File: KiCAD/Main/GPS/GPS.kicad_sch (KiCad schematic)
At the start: 16 parts, among them U1 MAX-M8Q, U2 PHA-23LN

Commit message: Fix labeling issue
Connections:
- net GPS RESET renamed GPS_RESET
- net GPS UART RX renamed GPS_UART_RX
- net GPS UART TX renamed GPS_UART_TX
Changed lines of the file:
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@@
 		)
 	)
-	(global_label "GPS UART TX"
+	(hierarchical_label "GPS_UART_TX"
 		(shape input)
 		(at 73.66 68.58 180)
-		(fields_autoplaced yes)
 		(effects
 			(font
@@
 			(justify right)
 		)
-		(property "Intersheetrefs" "${INTERSHEET_REFS}"
-			(at 58.1563 68.58 0)
-			(effects
-				(font
-					(size 1.27 1.27)
-				)
-				(justify right)
-				(hide yes)
-			)
-		)
 	)
-	(global_label "GPS UART RX"
+	(hierarchical_label "GPS_RESET"
 		(shape input)
-		(at 73.66 66.04 180)
-		(fields_autoplaced yes)
+		(at 80.01 88.9 180)
 		(effects
 			(font
@@
 			(justify right)
 		)
-		(property "Intersheetrefs" "${INTERSHEET_REFS}"
-			(at 57.8539 66.04 0)
-			(effects
-				(font
-					(size 1.27 1.27)
-				)
-				(justify right)
-				(hide yes)
-			)
-		)
 	)
-	(global_label "GPS RESET"
+	(hierarchical_label "GPS_UART_RX"
 		(shape input)
-		(at 80.01 88.9 180)
-		(fields_autoplaced yes)
+		(at 73.66 66.04 180)
 		(effects
 			(font
@@
 			(justify right)
 		)
-		(property "Intersheetrefs" "${INTERSHEET_REFS}"
-			(at 66.5626 88.9 0)
-			(effects
-				(font
-					(size 1.27 1.27)
-				)
-				(justify right)
-				(hide yes)
-			)
-		)
 	)

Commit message: Continue integrating
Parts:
- added AE2: Antenna, symbol Device:Antenna
- added C12: 0.001u, symbol Device:C
- added C13, C15, C16: 0.1u, symbol Device:C
- added C14: 0.01u, symbol Device:C
- added C17: 1.2p, symbol Device:C
- added IC1: E22-900M22S, E22-900M22S:E22-900M22S, symbol E22-900M22S:E22-900M22S
- added L3: 0.68u, symbol Device:L
- added L4: 1n, symbol Device:L
- added R5: 1.21k, symbol Device:R
- added U7: PHA-23LN, Package_TO_SOT_SMD:SOT-89-3, symbol RF_Amplifier:PHA-23LN
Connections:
- net GND: now also C13.1, C14.1, C17.2, L3.1, U7.2 (GND)
- new net: C13.2, C14.2, IC1.9 (VCC)
- new net: C15.1, R5.1
- new net: C12.2, L3.2, R5.2, U7.3
- new net: AE2.1 (A), C17.1, L4.2
- new net: C12.1, IC1.21 (ANT)
- new net: C15.2, C16.2, U7.1
- new net: C16.1, L4.1
- new net: IC1.1 (GND), IC1.10 (GND), IC1.11 (GND), IC1.12 (GND), IC1.2 (GND), IC1.20 (GND), IC1.22 (GND), IC1.3 (GND), IC1.4 (GND), IC1.5 (GND)
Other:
- moved on the sheet: AE1, C1, C2, C3, C4, C5, C6, JP1, L1, L2, R1, R2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

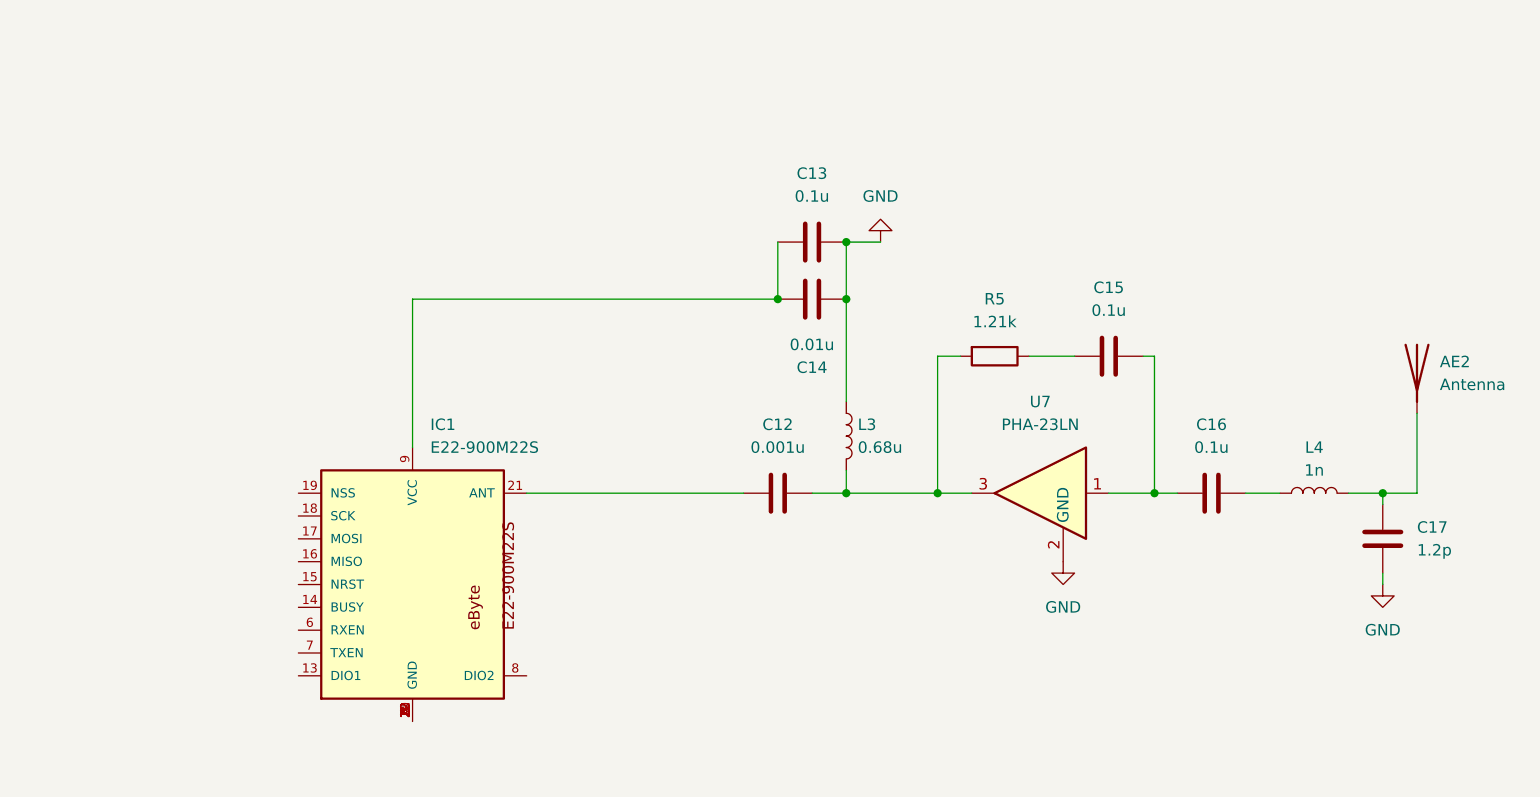
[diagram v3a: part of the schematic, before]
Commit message: Stable update. Begin fixing previous commit errors
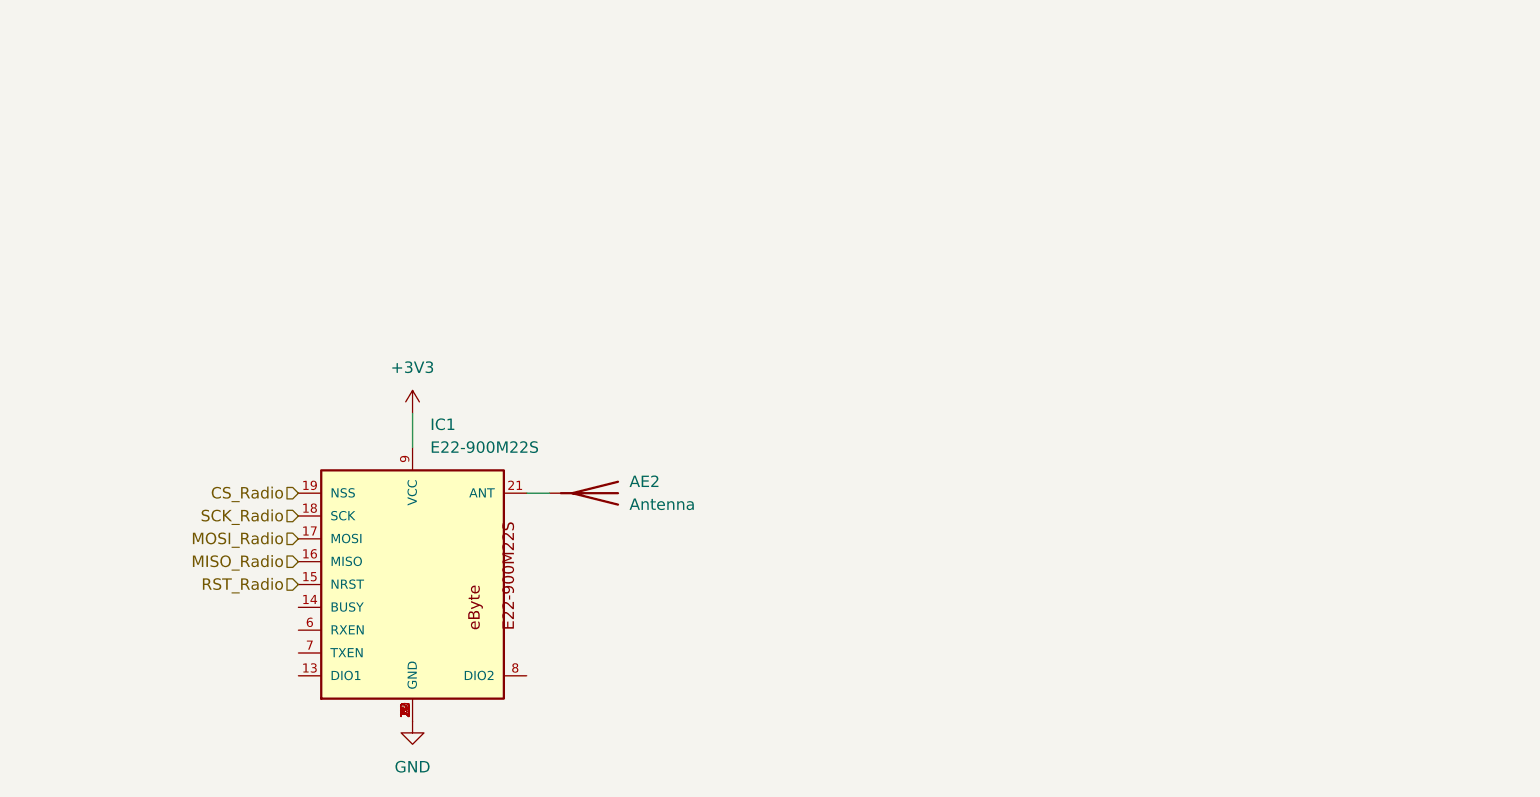
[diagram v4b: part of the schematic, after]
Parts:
- removed C12: 0.001u, symbol Device:C
- removed C13, C15, C16: 0.1u, symbol Device:C
- removed C14: 0.01u, symbol Device:C
- removed C17: 1.2p, symbol Device:C
- removed L3: 0.68u, symbol Device:L
- removed L4: 1n, symbol Device:L
- removed R5: 1.21k, symbol Device:R
- removed U7: PHA-23LN, Package_TO_SOT_SMD:SOT-89-3, symbol RF_Amplifier:PHA-23LN
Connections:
- net +3V3: now also IC1.9 (VCC)
- net GND: now also IC1.1 (GND), IC1.10 (GND), IC1.11 (GND), IC1.12 (GND), IC1.2 (GND), IC1.20 (GND), IC1.22 (GND), IC1.3 (GND), IC1.4 (GND), IC1.5 (GND)
- net at AE2.1 (A): now also IC1.21 (ANT)
- net RST_Radio: now reaches IC1.15 (NRST)
- net MISO_Radio: now reaches IC1.16 (MISO)
- net MOSI_Radio: now reaches IC1.17 (MOSI)
- net SCK_Radio: now reaches IC1.18 (SCK)
- net CS_Radio: now reaches IC1.19 (NSS)
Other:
- moved on the sheet: AE2

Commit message: Add new rf
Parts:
- removed AE2: Antenna, symbol Device:Antenna
- removed IC1: E22-900M22S, E22-900M22S:E22-900M22S, symbol E22-900M22S:E22-900M22S

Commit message: post meeting update
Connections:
- net at R4.1: now also U1.17 (SCL); no longer U1.2 (TXD)
- net at U1.16 (SDA): now also R3.1
- net at U1.3 (RXD): no longer R3.1
- net GPS_UART_RX renamed GPS_SDA
- net GPS_UART_TX renamed GPS_SCL
- no-connect marks 0 -> 4
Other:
- moved on the sheet: AE1, C1, C2, C3, C4, C5, C6, JP1, L1, L2, R1, R2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

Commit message: prep for merge
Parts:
- added JP2: LNA_ON/OFF, symbol Jumper:SolderJumper_2_Open
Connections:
- net +3V3: now also JP2.2 (B)
- net at R2.1, U1.13 (LNA_EN): now also JP2.1 (A)
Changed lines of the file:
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@@
+	)
+	(junction
+		(at 116.84 101.6)
+		(diameter 0)
+		(color 0 0 0 0)
 	)
 	(junction
@@
 	)
 	(junction
-		(at 116.84 101.6)
-		(diameter 0)
-		(color 0 0 0 0)
-	)
-	(junction
 		(at 184.15 106.68)
 		(diameter 0)
@@
 	(wire
 		(pts
+			(xy 116.84 101.6) (xy 127 101.6)
+		)
+		(stroke
+			(width 0)
+			(type default)
+		)
+	)
+	(wire
+		(pts
 			(xy 160.02 106.68) (xy 163.83 106.68)
 		)
@@
 	(wire
 		(pts
-			(xy 116.84 101.6) (xy 132.08 101.6)
-		)
-		(stroke
-			(width 0)
-			(type default)
-		)
-	)
-	(wire
-		(pts
 			(xy 213.36 106.68) (xy 209.55 106.68)
 		)
@@
 	(wire
 		(pts
+			(xy 137.16 101.6) (xy 137.16 93.98)
+		)
+		(stroke
+			(width 0)
+			(type default)
+		)
+	)
+	(wire
+		(pts
 			(xy 162.56 91.44) (xy 160.02 91.44)
 		)
@@
 		(pts
 			(xy 170.18 91.44) (xy 175.26 91.44)
+		)
+		(stroke
+			(width 0)
+			(type default)
+		)
+	)
+	(wire
+		(pts
+			(xy 134.62 101.6) (xy 137.16 101.6)
 		)
 		(stroke
@@
 					(unit 1)
 				)
+			)
+		)
+	)
+	(symbol
+		(lib_id "Jumper:SolderJumper_2_Open")
+		(at 130.81 101.6 0)
+		(unit 1)
+		(exclude_from_sim no)
+		(in_bom no)
+		(on_board yes)
+		(dnp no)
+		(property "Reference" "JP2"
+			(at 130.81 95.25 0)
+			(effects
+				(font
+					(size 1.27 1.27)
+				)
+			)
+		)
+		(property "Value" "LNA_ON/OFF"
+			(at 130.81 97.79 0)
+			(effects
+				(font
+					(size 1.27 1.27)
+				)
+			)
+		)
+		(property "Footprint" ""
+			(at 130.81 101.6 0)
+			(effects
+				(font
+					(size 1.27 1.27)
+				)
+				(hide yes)
+			)
+		)
+		(property "Datasheet" "~"
+			(at 130.81 101.6 0)
+			(effects
+				(font
+					(size 1.27 1.27)
+				)
+				(hide yes)
+			)
+		)
+		(property "Description" "Solder Jumper, 2-pole, open"
+			(at 130.81 101.6 0)
+			(effects
+				(font
+					(size 1.27 1.27)
+				)
+				(hide yes)
+			)
+		)
+		(pin "1"
+		)
+		(pin "2"
+		)
+		(instances
+			(project ""
+				(path "/bbb10697-a5dd-43b8-9c6f-4c5919cf3463/aff6795e-9a09-4ffe-99fb-dba81cca4540"
+					(reference "JP2")
+					(unit 1)
+				)
+			)
+		)
+	)
+	(symbol
+		(lib_id "power:+3V3")
+		(at 137.16 93.98 0)
+		(unit 1)
+		(exclude_from_sim no)
+		(in_bom yes)
+		(on_board yes)
+		(dnp no)
+		(fields_autoplaced yes)
+		(property "Reference" "#PWR033"
+			(at 137.16 97.79 0)
+			(effects
+				(font
+					(size 1.27 1.27)
+				)
+				(hide yes)
+			)
+		)
+		(property "Value" "+3V3"
+			(at 137.16 88.9 0)
+			(effects
+				(font
+					(size 1.27 1.27)
+				)
+			)
+		)
+		(property "Footprint" ""
+			(at 137.16 93.98 0)
+			(effects
+				(font
+					(size 1.27 1.27)
+				)
+				(hide yes)
+			)
+		)
+		(property "Datasheet" ""
+			(at 137.16 93.98 0)
+			(effects
+				(font
+					(size 1.27 1.27)
+				)
+				(hide yes)
+			)
+		)
+		(property "Description" "Power symbol creates a global label with name \"+3V3\""
+			(at 137.16 93.98 0)
+			(effects
+				(font
+					(size 1.27 1.27)
+				)
+				(hide yes)
+			)
+		)
+		(pin "1"
+		)
+		(instances
+			(project ""
+				(path "/bbb10697-a5dd-43b8-9c6f-4c5919cf3463/aff6795e-9a09-4ffe-99fb-dba81cca4540"
+					(reference "#PWR033")
+					(unit 1)
+				)
